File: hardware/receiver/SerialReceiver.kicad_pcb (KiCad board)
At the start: 2 copper layers, 78.7 x 70.5 mm, 46 parts, among them J1 DATA, J2 CONTROL, J3 RX, J4 Clock select, J5 LED enable, J6 Mode select, Q1 2N7000, Q2 2N7000, SW1 SW_Push, U1 74HC132, U2 74HC191, U3 74HC191, U4 74HC595, U5 74HC74, U6 74LS244

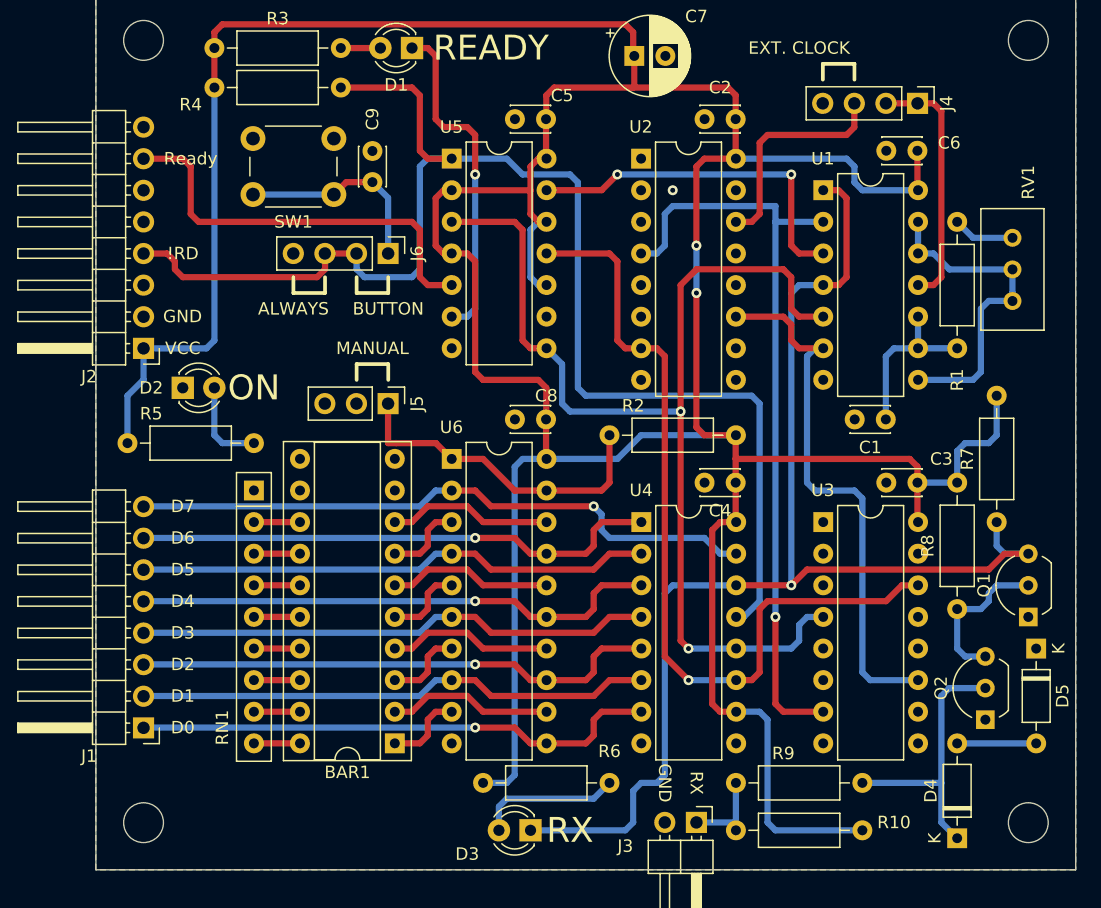
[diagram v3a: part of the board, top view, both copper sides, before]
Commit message: The receiver's PCB is finished.
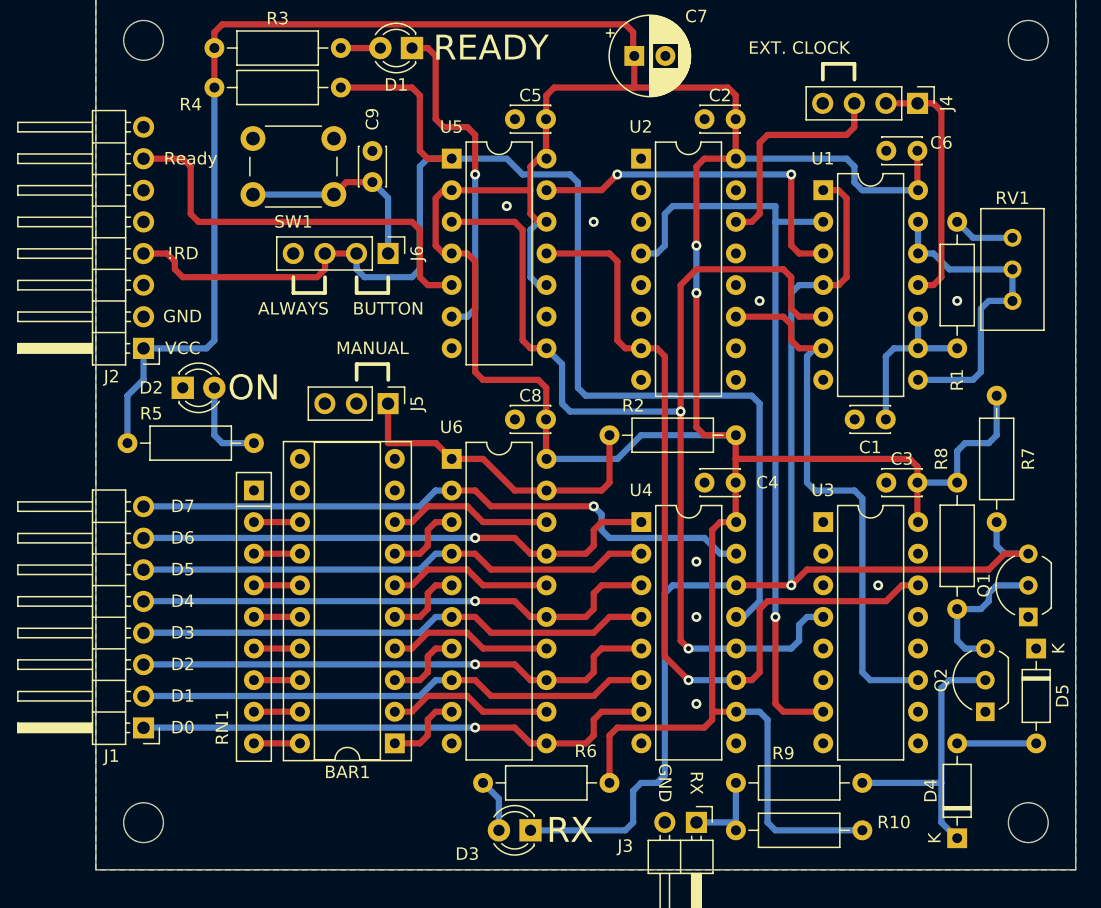
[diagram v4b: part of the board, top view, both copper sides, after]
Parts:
- moved R6 10.2 mm to (160.7, 125.7), turned to 180 degrees
- moved Q2 0.64 mm to (190.9, 120.0)
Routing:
- net VCC: track 323.7 -> 306.9 mm
- net Net-(D3-Pad2): track 11.6 -> 4.34 mm
- net Net-(D4-Pad1): track 22.1 -> 22.7 mm
- net Net-(Q1-Pad2): track 12.6 -> 11.9 mm
- net GND: vias 1 -> 8

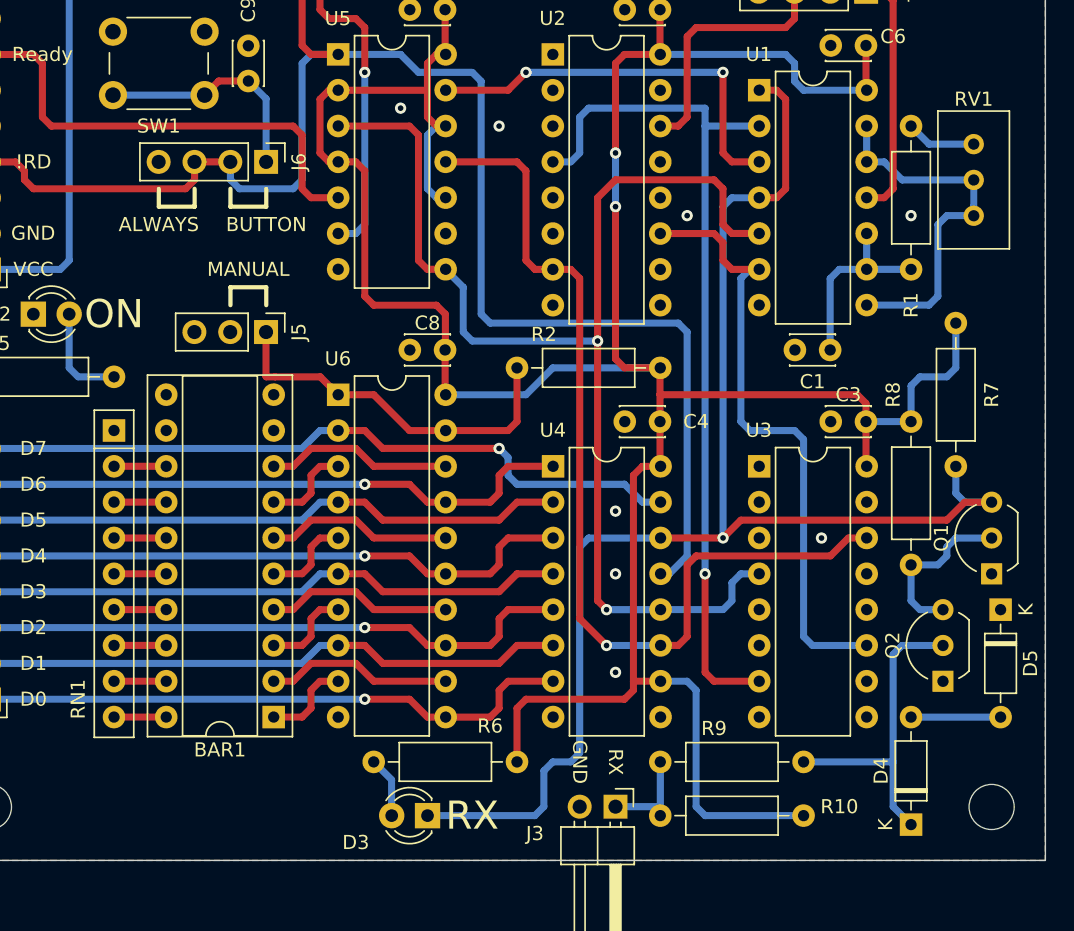
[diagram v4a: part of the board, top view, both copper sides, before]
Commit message: The schematic and the PCB is finished.
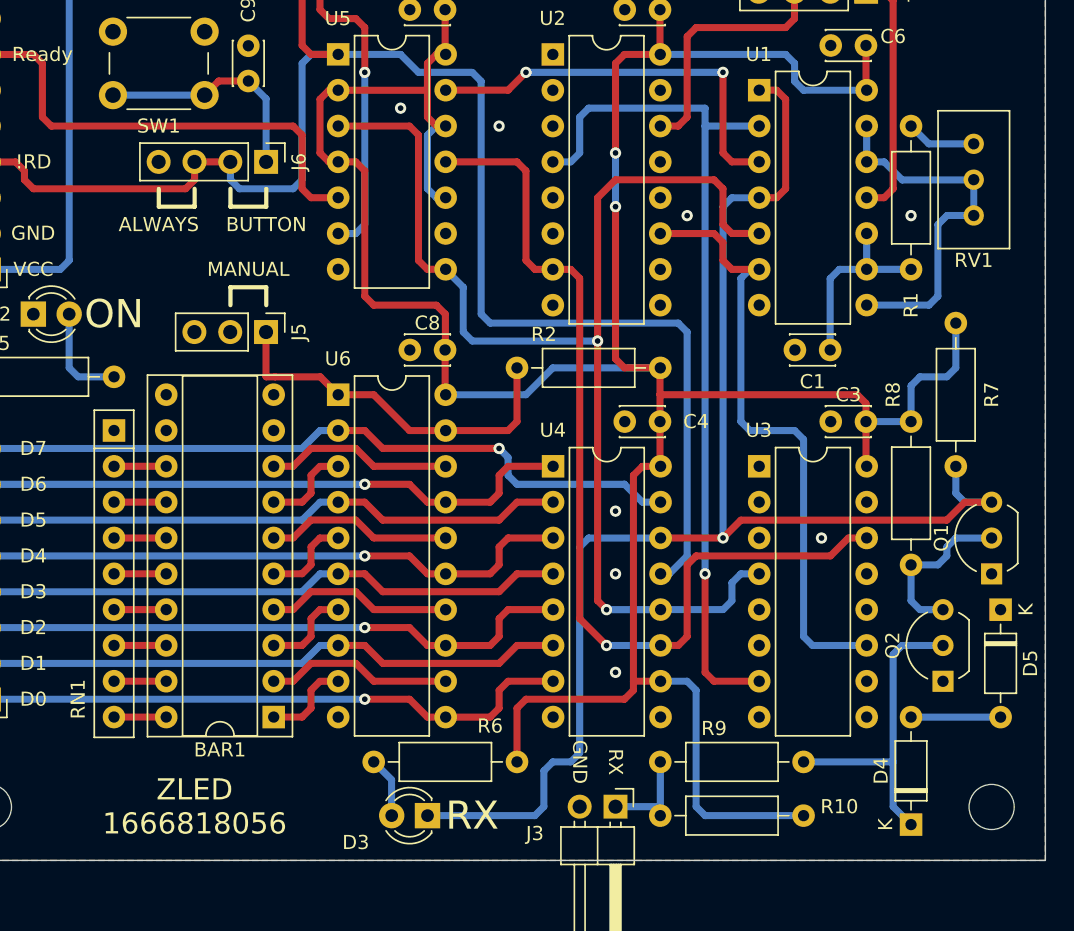
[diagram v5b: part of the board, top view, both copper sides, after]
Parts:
- D4, D5: value D_Zener -> 15V
- R7: value 10k -> 1k
- moved RV1 5.10 mm to (193.0, 81.9), turned to 90 degrees
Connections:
- RV1 pad 1: Net-(RV1-Pad1) -> Net-(R1-Pad2)
- RV1 pad 2: Net-(RV1-Pad1) -> Net-(U1-Pad12)
- RV1 pad 3: Net-(R1-Pad2) -> Net-(U1-Pad12)
- U1 pad 12: Net-(RV1-Pad1) -> Net-(U1-Pad12)
- U1 pad 13: Net-(RV1-Pad1) -> Net-(U1-Pad12)
- U1 pad 8: Net-(RV1-Pad1) -> Net-(U1-Pad12)
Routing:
- net Net-(RV1-Pad1): track 26.4 -> 0.00 mm
- net Net-(U1-Pad12): track 0.00 -> 26.4 mm
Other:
- board text added: "ZLED 1666818056"

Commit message: Minor fixes on the receiver's PCB.
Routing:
- net VCC: vias 1 -> 2
- net (no net): vias 1 -> 0
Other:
- board text added: "ZLED 1667060396"
- board text removed: "ZLED 1666818056"
